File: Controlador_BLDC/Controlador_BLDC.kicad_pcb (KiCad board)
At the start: 4 copper layers, 70 x 90 mm, 97 parts, among them IC1 AP1509-50SG-13, IC2 LMS8117AMP-3.3_NOPB, J1 Conn_01x05, J2 MOTOR, U1 LM339DR, U2 EK-TM4C123GXL, U3 IR2301SPBF, U4 IR2301SPBF, U5 IR2301SPBF

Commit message: Versió definitiva de la placa
S'ha fet una revisió de la placa i s'ha canviatt models i disseny en general. És la placa que s'ha enviat a fabricar
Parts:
- removed H4: MountingHole, MountingHole:MountingHole_4.3mm_M4_ISO14580
- removed U2: EK-TM4C123GXL, TIVA-Modfied:MODULE_EK-TM4C123GXL_mofied
- removed U3, U4, U5: IR2301SPBF, IR2301SPBF:SOIC8L_INF
- added IC3: LM339D, LM339D:SOIC127P600X175-14N, B.Cu at (195.1, 94.4)
- added IC4: IR2301SPBF, IR2301SPBF_modifed:SOIC127P600X175-8N, F.Cu at (212.2, 45.0)
- added IC5: IR2301SPBF, IR2301SPBF_modifed:SOIC127P600X175-8N, F.Cu at (212.6, 31.7)
- added IC6: IR2301SPBF, IR2301SPBF_modifed:SOIC127P600X175-8N, F.Cu at (212.2, 59.1)
- added J3: Conn_01x01_Pin, Connector_PinHeader_2.54mm:PinHeader_1x01_P2.54mm_Vertical, F.Cu at (180.5, 71.1)
- added J_TP6: Conn_01x02_Pin, Connector_PinHeader_2.54mm:PinHeader_1x02_P2.54mm_Vertical, F.Cu at (168.7, 29.8)
- CAH1, CBH1, CCH1, RAH1, RBH1, RCH1: moved to B.Cu
- CAL1, CBL1, CCL1, RAL1, RBL1, RCL1: moved to F.Cu
- H1, H2, H3: footprint MountingHole:MountingHole_4.3mm_M4_ISO14580 -> MountingHole:MountingHole_3.2mm_M3
- J_DC1: footprint TerminalBlock:TerminalBlock_bornier-2_P5.08mm -> TerminalBlock_Phoenix:TerminalBlock_Phoenix_MKDS-1,5-2-5.08_1x02_P5.08mm_Horizontal
- J_TP3: value Conn_01x03_Pin -> Conn_01x04_Pin; footprint Connector_PinHeader_2.54mm:PinHeader_1x03_P2.54mm_Vertical -> Connector_PinHeader_2.54mm:PinHeader_1x04_P2.54mm_Vertical
- J_TP5: value Conn_01x04_Pin -> Conn_01x03_Pin; footprint Connector_PinHeader_2.54mm:PinHeader_1x04_P2.54mm_Vertical -> Connector_PinHeader_2.54mm:PinHeader_1x03_P2.54mm_Vertical
- J_TPG1, J_TPG2, J_TPG3: value Conn_01x02_Pin -> Conn_01x04_Pin; footprint Connector_PinHeader_2.54mm:PinHeader_1x02_P2.54mm_Vertical -> Connector_PinHeader_2.54mm:PinHeader_1x04_P2.54mm_Vertical
- L1: value CDRH127_LDNP-470MC -> 744770147; footprint CDRH127-LDNP-470MC:INDPM120120X800N -> 744770147:WE-PD_1260_1245_1280_121054
- RPOT1: footprint TerminalBlock:TerminalBlock_bornier-3_P5.08mm -> TerminalBlock_Phoenix:TerminalBlock_Phoenix_MKDS-1,5-3-5.08_1x03_P5.08mm_Horizontal
- U1: value LM339DR -> EK-TM4C123GXL; footprint LM339DR:D14 -> TIVA-Modfied:MODULE_EK-TM4C123GXL_mofied; moved to F.Cu
- moved H3 29.8 mm to (194.2, 107.0)
- moved D2 27.4 mm to (209.8, 36.2)
- moved Cb2 17.7 mm to (197.1, 86.1), turned to 90 degrees
- moved Cb3 17.7 mm to (201.5, 86.1), turned to 90 degrees
- moved CLDO1 16.4 mm to (176.7, 74.1), turned to 0 degrees
- moved Cb1 16.3 mm to (192.8, 86.0), turned to 90 degrees
- moved IC2 15.8 mm to (178.0, 79.6)
- moved D3 14.1 mm to (209.5, 63.6)
- moved D4 13.2 mm to (209.6, 49.4)
- moved CLDO2 12.8 mm to (177.8, 85.4), turned to 180 degrees
- moved J_TP5 12.6 mm to (196.4, 71.1)
- moved RPull3 12.5 mm to (206.3, 103.4), turned to -90 degrees
- moved U1 12.3 mm to (191.1, 106.8), turned to 180 degrees
- moved CBD1 11.2 mm to (162.6, 67.8)
- moved IC1 11.2 mm to (166.7, 72.1)
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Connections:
- D2 pad 1: VBA -> VBC
- D3 pad 1: VBB -> VBA
- D4 pad 1: VBC -> VBB
- J_TP3 pad 1: FASE_B -> Neu_div
- J_TP3 pad 2: B_BEMF -> FASE_C
- J_TP3 pad 3: Neu -> C_BEMF
- J_TP5 pad 1: Neu_div -> FASE_B
- J_TP5 pad 2: FASE_C -> B_BEMF
- J_TP5 pad 3: C_BEMF -> Neu
- J_TPG1 pad 2: GND -> MGHC
- J_TPG2 pad 2: GND -> MGHB
- J_TPG3 pad 2: GND -> MGHA
- MOSFET1 pad 1: /RGHA -> MGHA
- MOSFET2 pad 1: /RGLA -> MGLA
- MOSFET3 pad 1: /RGHB -> MGHB
- MOSFET4 pad 1: /RGLB -> MGLB
- MOSFET5 pad 1: /RGHC -> MGHC
- MOSFET6 pad 1: /RGLC -> MGLC
- RGAH1 pad 1: /RGHA -> MGHA
- RGAL1 pad 1: /RGLA -> MGLA
- RGBH1 pad 1: /RGHB -> MGHB
- RGBL1 pad 1: /RGLB -> MGLB
- RGCH1 pad 1: /RGHC -> MGHC
- RGCL1 pad 1: /RGLC -> MGLC
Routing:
- net SPI_CS: track 89.7 -> 5.70 mm, vias 3 -> 0
- net SPI_MOSI: track 14.0 -> 87.1 mm
- net GND: track 68.9 -> 105.1 mm, vias 240 -> 312
- net +5V: track 75.3 -> 44.0 mm, vias 9 -> 7
- net FASE_C: track 127.1 -> 97.5 mm
- net FASE_A: track 92.2 -> 69.2 mm, vias 6 -> 7
- net FASE_B: track 105.3 -> 84.0 mm
- net Neu_div: track 88.9 -> 71.7 mm
- net A_BEMF: track 45.5 -> 30.0 mm
- net B_BEMF: track 40.5 -> 26.7 mm
- net MGLA: track 0.00 -> 12.1 mm
- net MGLB: track 0.00 -> 12.0 mm
- net MGLC: track 0.00 -> 11.9 mm
- net Neu: track 38.7 -> 48.5 mm
- net MGHC: track 0.00 -> 8.87 mm
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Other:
- board text added: "Jordi Godàs Pep Puig LSE 2026/2027"
- board text added: "MGHA"
- board text added: "MGHB"
- board text added: "MGHC"
- board text added: "MGLA"
- board text added: "MGLB"
- board text added: "MGLC"
- board text added: "VCC"

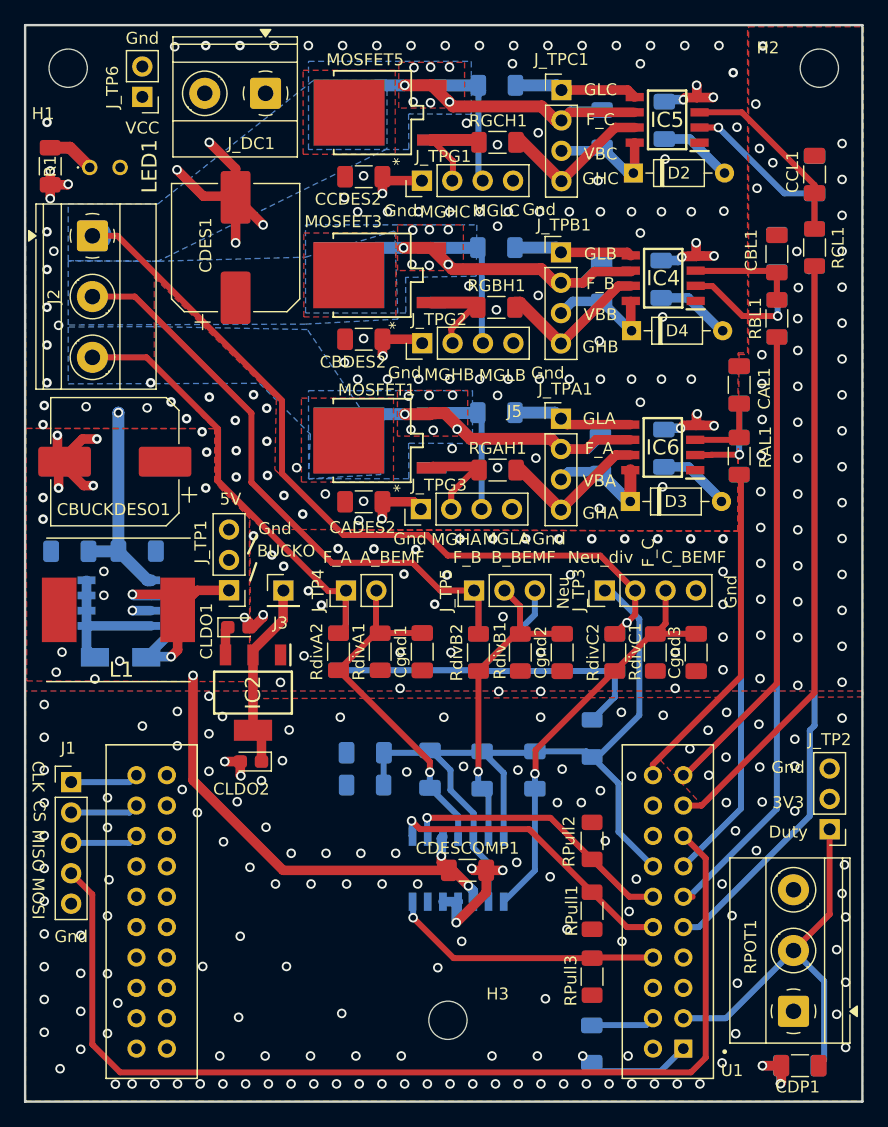
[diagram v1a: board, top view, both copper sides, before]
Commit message: Versió final**
S'ha corretgit el problema de DRC indicat pel profesor a les capes de coure a les fases
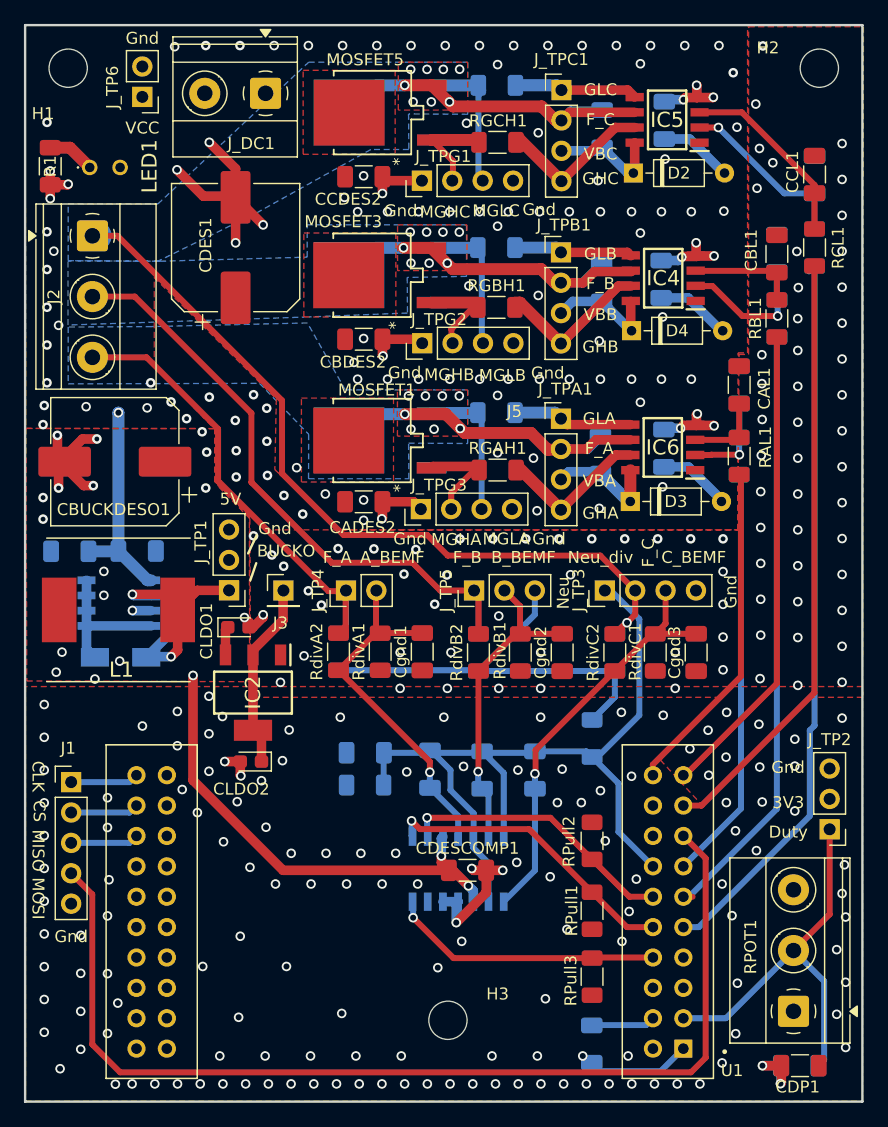
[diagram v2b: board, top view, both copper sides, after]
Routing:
- net FASE_A: track 69.2 -> 69.1 mm, vias 7 -> 8
- net VCC: vias 27 -> 28
- net GND: vias 312 -> 310
- net FASE_C: vias 8 -> 9
- net FASE_B: vias 7 -> 8
